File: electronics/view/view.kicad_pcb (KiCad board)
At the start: 2 copper layers, 81.2 x 81.2 mm, 90 parts, among them J1 BLDC, J2 USB_C_Receptacle_USB2.0, J3 LCD, J4 Strain, J5 Strain, Q1 MMBT4403, Q2 UMH3N, U1 MT6701-CT, U2 T-Micro32_Plus, U3 CH340C, U4 HX711, U5 TMC6300, U6 AP1117-33, U7 SN74LV1T34DBV, U8 VEML7700

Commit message: View: PCB checkpoint
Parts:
- R10, R11, R12, R7, R8, R9: value 100k -> 10k
- TP1, TP10, TP11, TP12, TP2, TP3, TP4, TP5, TP6, TP7, TP8, TP9: moved to B.Cu
- moved TP11 95.2 mm to (-29.5, 16.0)
- moved TP9 91.1 mm to (-23.5, 16.0)
- moved TP12 88.4 mm to (-19.5, 8.50)
- moved TP10 87.2 mm to (-26.5, 16.0)
- moved TP3 65.0 mm to (19.0, 36.0)
- moved TP1 65.0 mm to (15.0, 36.0)
- moved TP4 59.5 mm to (-5.50, -38.0)
- moved TP2 57.7 mm to (23.0, 36.0)
- moved TP8 53.4 mm to (18.0, 21.5)
- moved TP5 51.5 mm to (5.50, -38.0)
- moved TP6 49.3 mm to (23.0, 16.5)
- moved TP7 44.2 mm to (20.5, 19.0)
- moved C20 8.06 mm to (2.00, 3.50), turned to 180 degrees
- moved C29 3.61 mm to (-32.5, 10.5)
- moved C26 2.50 mm to (-36.5, 18.0), turned to 180 degrees
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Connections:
- U2 pad 13: /TMC_WL -> /MAG_CSN
- U2 pad 14: /MAG_CLK -> /TMC_WL
- U2 pad 16: /MAG_CSN -> /MAG_CLK
- U2 pad 17: (no net) -> /MAG_DO
- U2 pad 22: /STRAIN_SCK -> /SCL
- U2 pad 23: /SCL -> /SDA
- U2 pad 24: /SDA -> /STRAIN_SCK
- U2 pad 5: /MAG_DO -> (no net)
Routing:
- net +3V3: track 0.00 -> 277.5 mm, vias 0 -> 12
- net +5V: track 70.1 -> 259.3 mm, vias 0 -> 6
- net /SCL: track 0.00 -> 107.7 mm, vias 0 -> 3
- net /SDA: track 0.00 -> 101.7 mm, vias 0 -> 3
- net /MAG_CLK: track 0.00 -> 57.3 mm, vias 0 -> 1
- net /TMC_DIAG: track 0.00 -> 57.0 mm
- net /STRAIN_SCK: track 0.00 -> 54.9 mm, vias 0 -> 2
- net GND: track 29.4 -> 84.3 mm, vias 45 -> 69
- net /STRAIN_DO: track 0.00 -> 54.5 mm, vias 0 -> 2
- net /MAG_CSN: track 0.00 -> 53.1 mm, vias 0 -> 1
- net /MAG_DO: track 0.00 -> 47.6 mm, vias 0 -> 1
- net /TMC_UL: track 0.00 -> 42.6 mm
- net /TMC_UH: track 0.00 -> 40.9 mm
- net /TMC_VH: track 0.00 -> 40.4 mm
- net /ESP32_BOOT: track 0.00 -> 33.2 mm, vias 0 -> 2
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- added copper zone on F.Cu, net +5V
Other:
- board text removed: "DO NOT OVER-TIGHTEN"

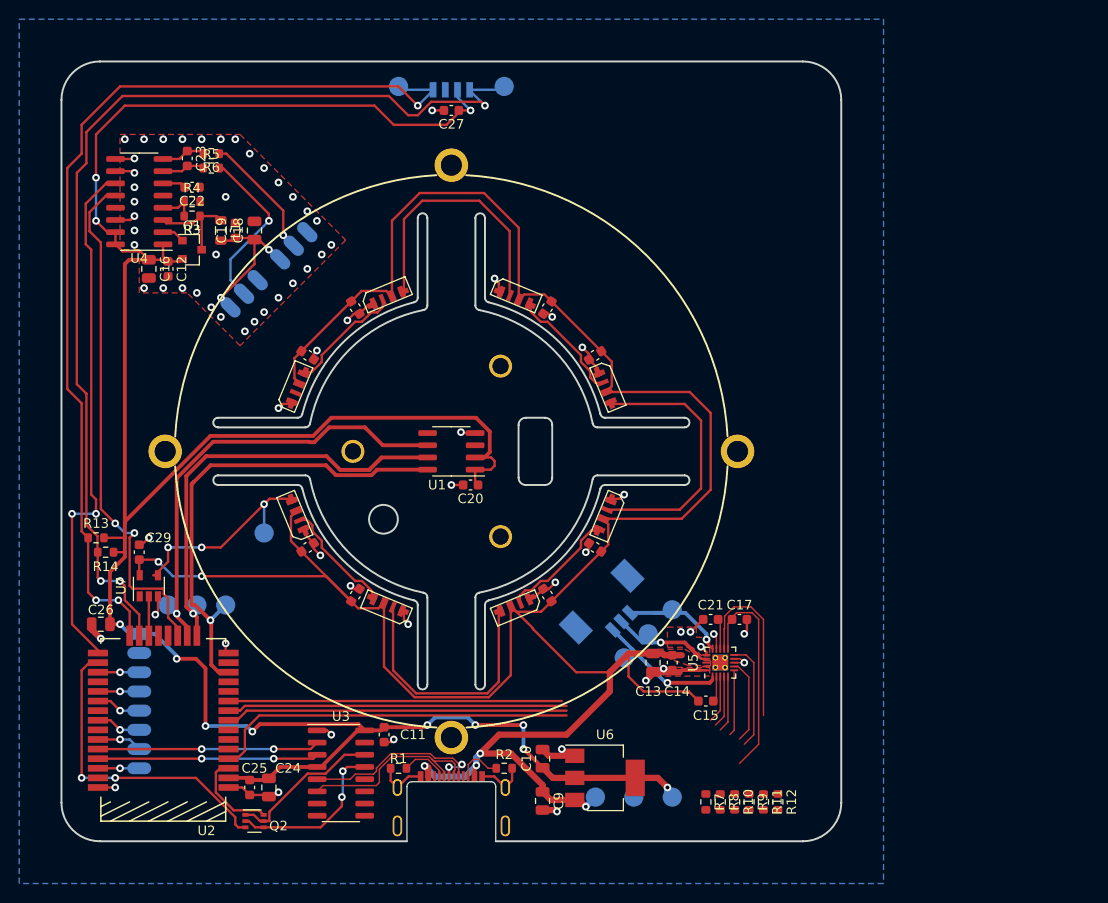
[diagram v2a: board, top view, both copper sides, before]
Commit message: View: finished initial routing
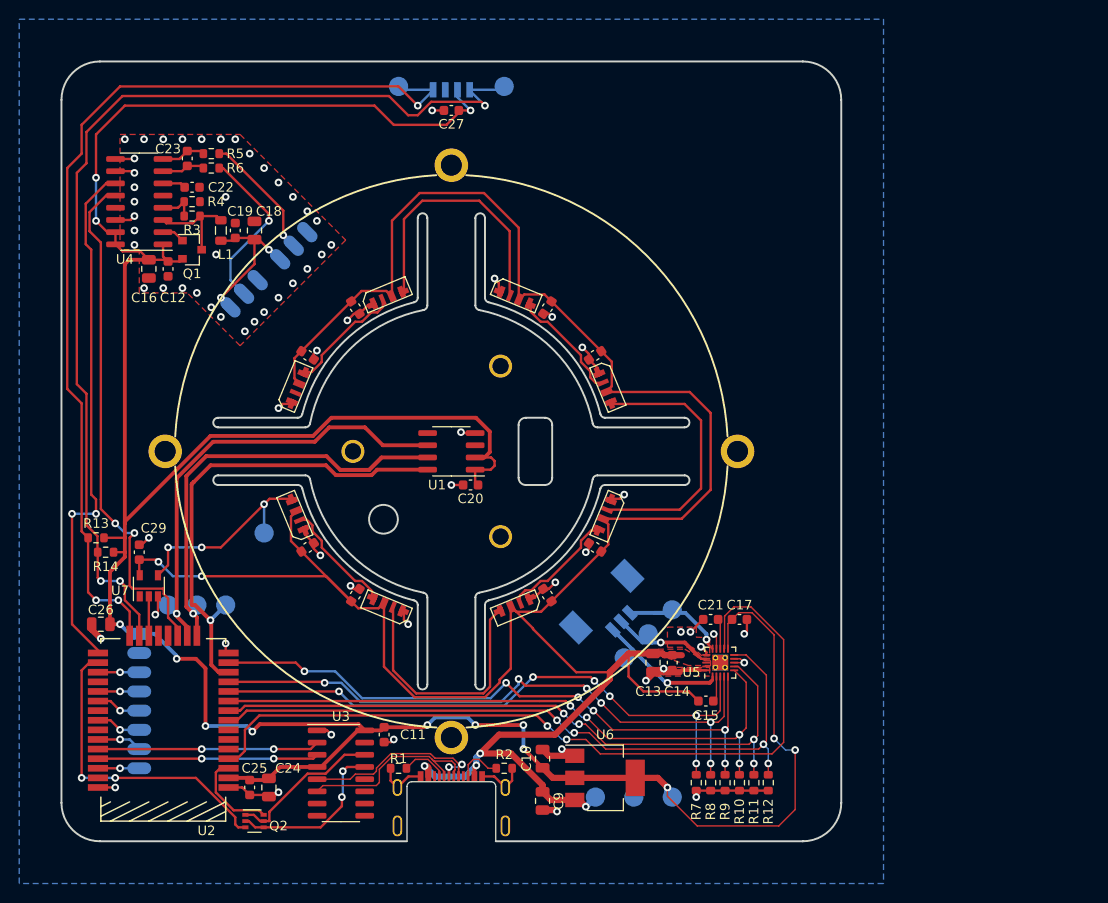
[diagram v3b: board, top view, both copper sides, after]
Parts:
- moved R9 3.20 mm to (28.5, 34.5)
- moved R11 2.24 mm to (31.5, 34.5)
- moved R12 2.24 mm to (33.0, 34.5)
- moved R7 2.24 mm to (25.5, 34.5)
- moved R8 2.24 mm to (27.0, 34.5)
- moved R10 2.06 mm to (30.0, 34.5)
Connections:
- R10 pad 1: /TMC_VL -> /TMC_UL
- R11 pad 1: /TMC_WH -> /TMC_WL
- R12 pad 1: /TMC_WL -> /TMC_VL
- R8 pad 1: /TMC_UL -> /TMC_VH
- R9 pad 1: /TMC_VH -> /TMC_WH
- U2 pad 10: /TMC_VH -> /TMC_UL
- U2 pad 11: /TMC_VL -> /TMC_UH
- U2 pad 12: /TMC_WH -> /TMC_VH
- U2 pad 14: /TMC_WL -> /TMC_WH
- U2 pad 8: /TMC_UH -> /TMC_VL
- U2 pad 9: /TMC_UL -> /TMC_WL
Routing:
- net /TMC_VL: track 11.3 -> 73.2 mm, vias 0 -> 4
- net /TMC_WL: track 8.83 -> 69.8 mm, vias 0 -> 4
- net /TMC_WH: track 5.88 -> 66.6 mm, vias 0 -> 6
- net /TMC_DIAG: track 57.0 -> 85.5 mm, vias 0 -> 2
- net /TMC_VH: track 40.4 -> 65.8 mm, vias 0 -> 6
- net /TMC_UL: track 42.6 -> 67.0 mm, vias 0 -> 4
- net /TMC_UH: track 40.9 -> 65.0 mm, vias 0 -> 6
- net +3V3: track 277.5 -> 299.7 mm, vias 12 -> 14
- net GND: track 84.3 -> 92.5 mm, vias 69 -> 70
- net +5V: track 259.3 -> 258.3 mm

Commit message: Cleanup
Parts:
- added R15: 2.2k, Resistor_SMD:R_0603_1608Metric, F.Cu at (-31.0, 8.00)
- added R16: 2.2k, Resistor_SMD:R_0603_1608Metric, F.Cu at (-30.0, 6.50)
- moved TP5 17.5 mm to (-12.0, -38.0)
- moved TP4 2.50 mm to (-8.00, -38.0)
- moved C11 0.50 mm to (-7.00, 30.0)
- moved C13 0.50 mm to (21.0, 22.5)
- moved C14 0.50 mm to (23.0, 22.5)
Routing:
- net /MAG_CLK: track 57.3 -> 47.0 mm
- net /SDA: track 101.7 -> 97.1 mm
- net /SCL: track 107.7 -> 104.2 mm, vias 3 -> 4
- net +5V: track 258.3 -> 255.1 mm, vias 6 -> 8
- net +3V3: track 299.7 -> 296.6 mm
- net GND: track 92.5 -> 90.3 mm
- net Net-(J1-Pad1): track 14.7 -> 16.0 mm
- net /MAG_DO: track 47.5 -> 48.7 mm
- net /MAG_CSN: track 53.1 -> 54.0 mm
- net /TMC_UH: track 65.0 -> 65.7 mm, vias 6 -> 4
- net /STRAIN_DO: track 54.5 -> 53.9 mm
- net /STRAIN_SCK: track 54.9 -> 55.5 mm
- net /TMC_VH: vias 6 -> 4
- net /TMC_VL: vias 4 -> 2
- net /TMC_UL: vias 4 -> 2
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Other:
- board text added: "SmartKnob View"
- board text added: "v0.1"

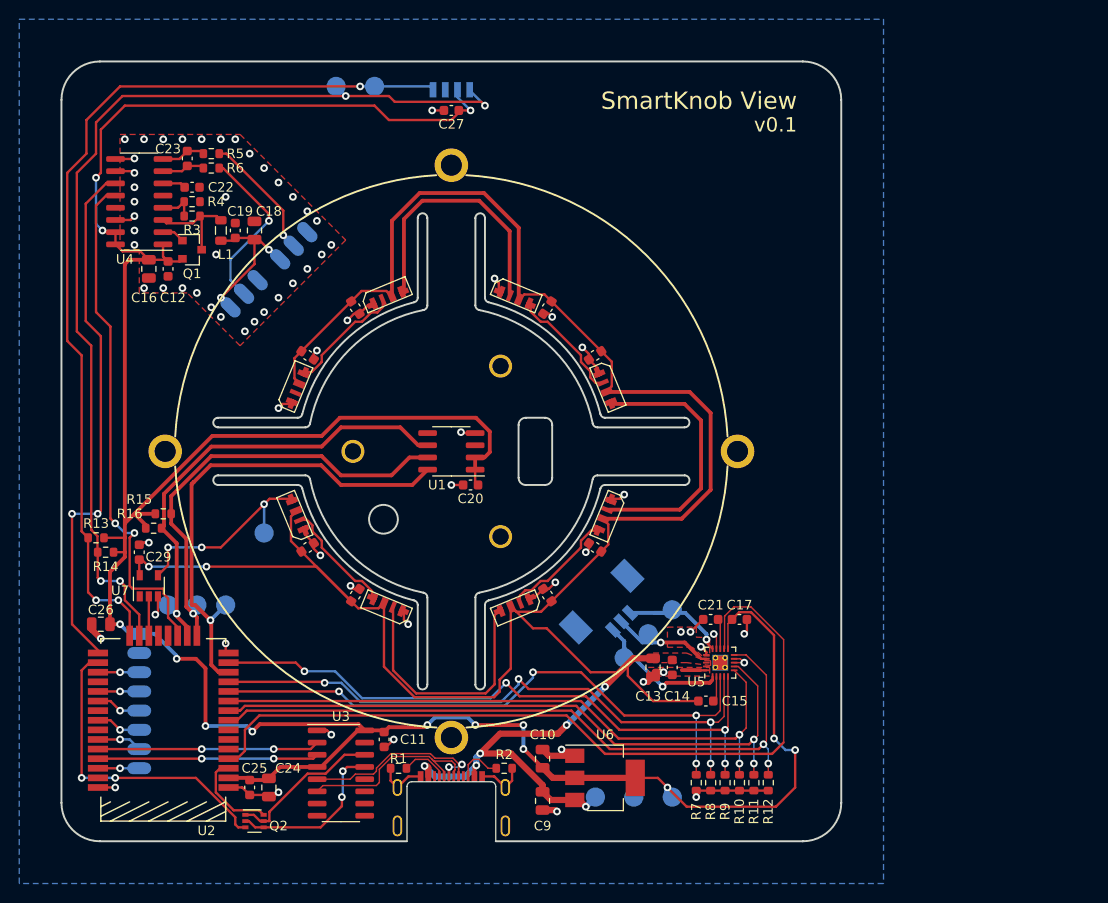
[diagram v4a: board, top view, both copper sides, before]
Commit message: View: Small pcb tweaks
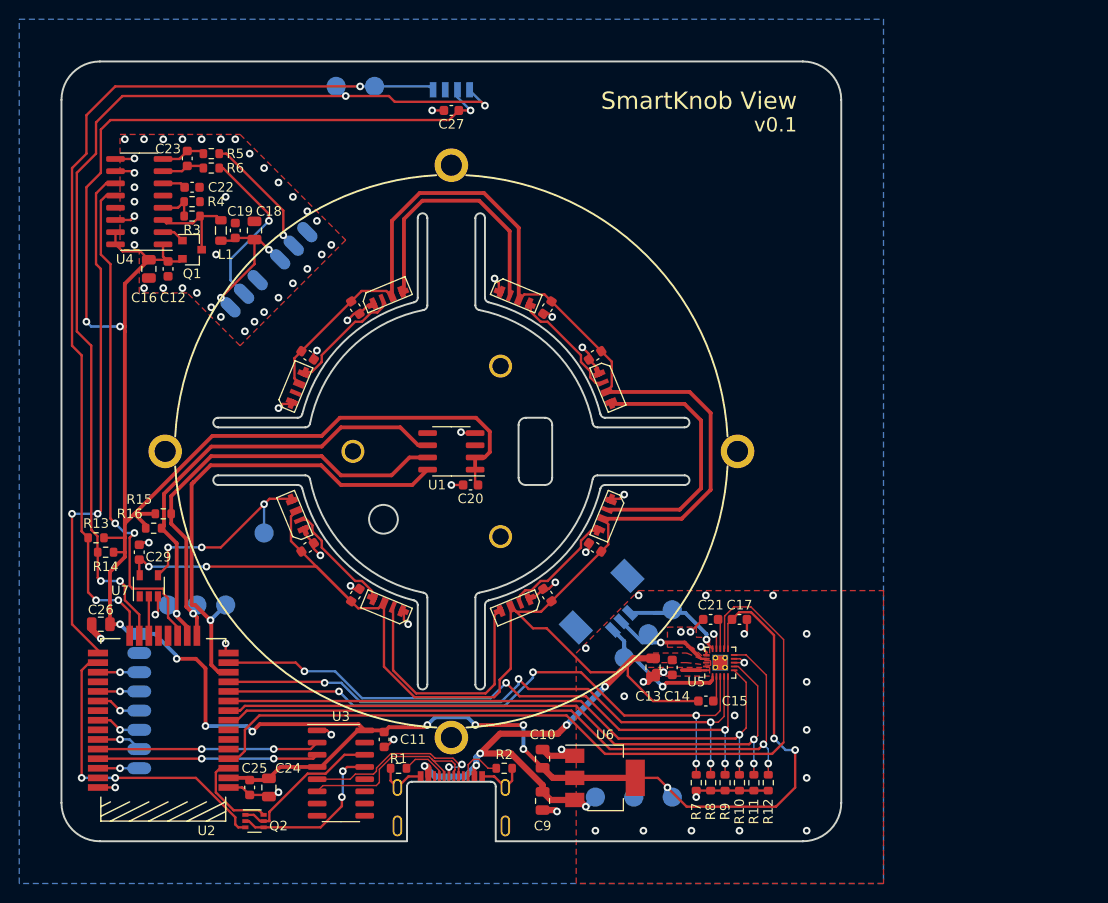
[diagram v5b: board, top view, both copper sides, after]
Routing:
- net +3V3: track 296.6 -> 306.4 mm
- net /STRAIN_SCK: track 55.5 -> 54.6 mm
- net GND: vias 70 -> 85

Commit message: View: Add initial screen pcb
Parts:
- J3: footprint view_custom:SolderPads_2mm_8 -> SolderPads:SolderPads_2mm_8
- J4, J5: footprint view_custom:SolderPads_2mm_3 -> SolderPads:SolderPads_2mm_3
